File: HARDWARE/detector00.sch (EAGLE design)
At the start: 12 parts, among them IC1 OPT1O1

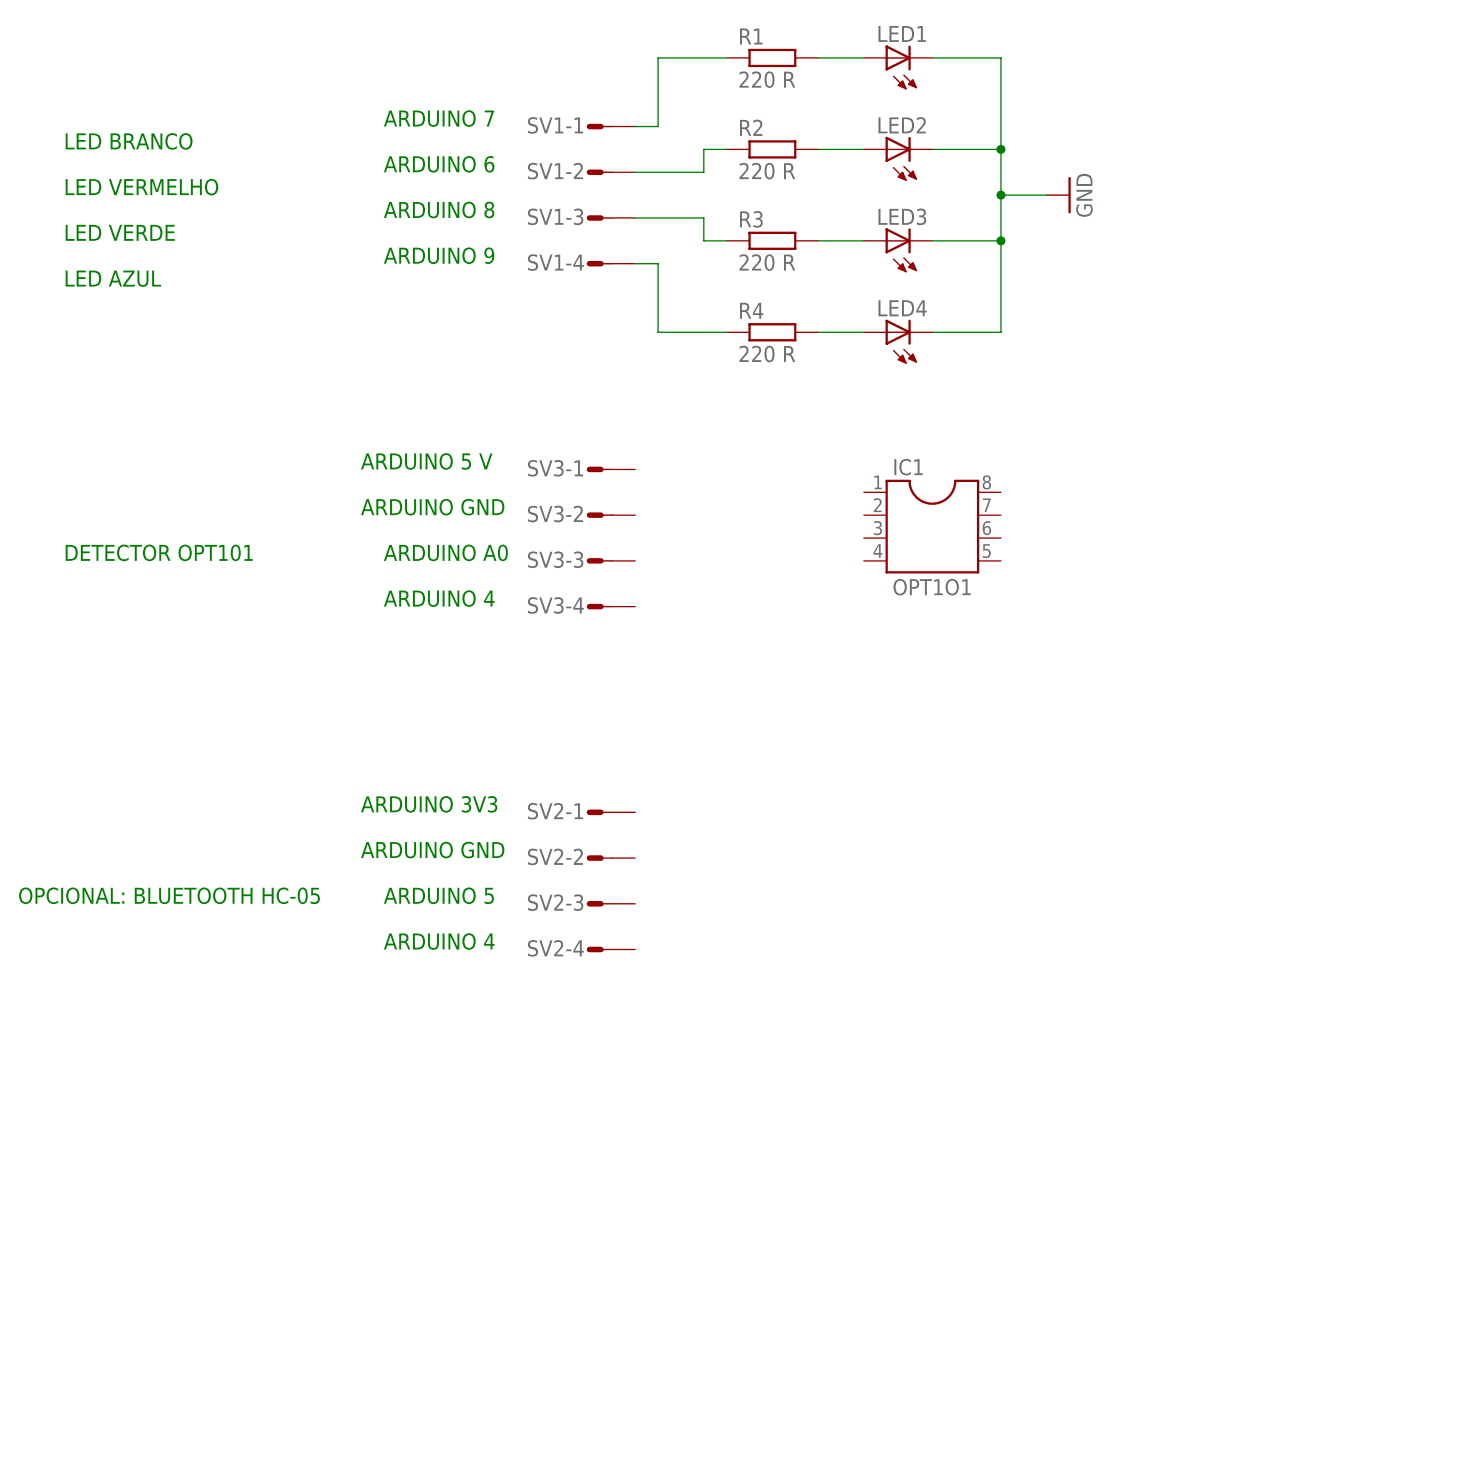
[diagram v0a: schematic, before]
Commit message: Adequações
-proteção ADC
-Correção detector00
-Adição detector05
-Inclusão de teste de tempo de leitura e de conjunto optoeletrônico
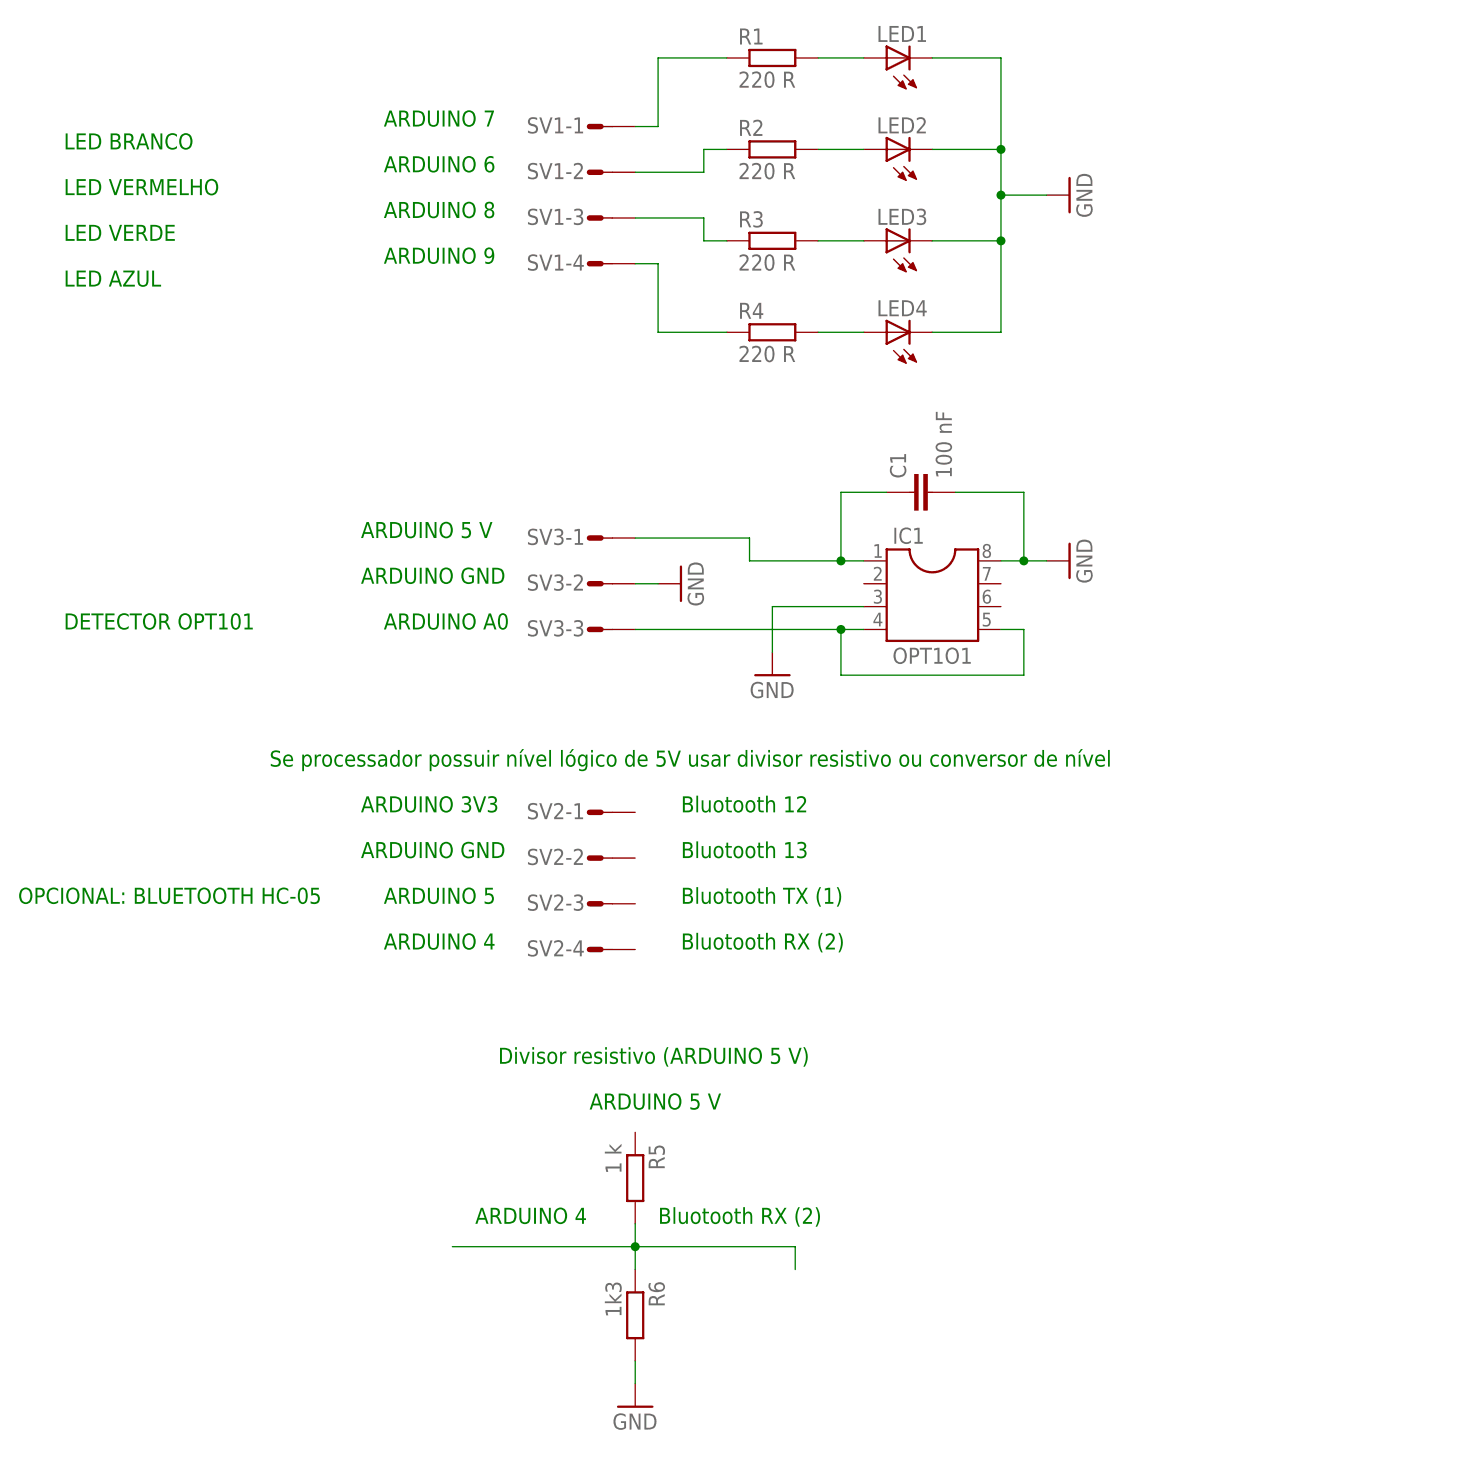
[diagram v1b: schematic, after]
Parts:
- added C1: 100 nF, rcl:C-EU050-035X075
- added R5: 1 k, rcl:R-EU_0204/7
- added R6: 1k3, rcl:R-EU_0204/7
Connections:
- new net N$3: C1.1, IC1.1, SV3-1.S
- new net N$4: R5.2, R6.1
- new net N$8: IC1.4, IC1.5, SV3-3.S
- net GND: now also C1.2, IC1.3, IC1.8, R6.2, SV3-2.S
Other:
- note added: "Bluotooth 12"
- note added: "Bluotooth 13"
- note added: "Bluotooth RX (2)"
- note added: "Bluotooth TX (1)"
- note added: "Divisor resistivo (ARDUINO 5 V)"
- note added: "Se processador possuir nível lógico de 5V usar divisor resistivo ou conversor de nível"
- moved on the sheet: IC1, SV3-1, SV3-2, SV3-3
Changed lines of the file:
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@@
 <part name="GND1" library="supply1" deviceset="GND" device=""/>
 <part name="IC1" library="ic-package" deviceset="DIL8" device="" value="OPT1O1"/>
+<part name="C1" library="rcl" deviceset="C-EU" device="050-035X075" value="100 nF"/>
+<part name="GND2" library="supply1" deviceset="GND" device=""/>
+<part name="GND3" library="supply1" deviceset="GND" device=""/>
+<part name="GND4" library="supply1" deviceset="GND" device=""/>
+<part name="R5" library="rcl" deviceset="R-EU_" device="0204/7" value="1 k"/>
+<part name="R6" library="rcl" deviceset="R-EU_" device="0204/7" value="1k3"/>
+<part name="GND5" library="supply1" deviceset="GND" device=""/>
 </parts>
 <sheets>
@@
 <text x="25.4" y="71.12" size="1.778" layer="91">LED BRANCO</text>
 <text x="25.4" y="60.96" size="1.778" layer="91">LED VERDE</text>
-<text x="58.42" y="35.56" size="1.778" layer="91">ARDUINO 5 V</text>
-<text x="58.42" y="30.48" size="1.778" layer="91">ARDUINO GND</text>
-<text x="60.96" y="25.4" size="1.778" layer="91">ARDUINO A0</text>
-<text x="60.96" y="20.32" size="1.778" layer="91">ARDUINO 4</text>
-<text x="25.4" y="25.4" size="1.778" layer="91">DETECTOR OPT101</text>
+<text x="58.42" y="27.94" size="1.778" layer="91">ARDUINO 5 V</text>
+<text x="58.42" y="22.86" size="1.778" layer="91">ARDUINO GND</text>
+<text x="60.96" y="17.78" size="1.778" layer="91">ARDUINO A0</text>
+<text x="25.4" y="17.78" size="1.778" layer="91">DETECTOR OPT101</text>
 <text x="25.4" y="66.04" size="1.778" layer="91">LED VERMELHO</text>
 <text x="25.4" y="55.88" size="1.778" layer="91">LED AZUL</text>
+<text x="93.98" y="-2.54" size="1.778" layer="91">Bluotooth 12</text>
+<text x="93.98" y="-7.62" size="1.778" layer="91">Bluotooth 13</text>
+<text x="93.98" y="-12.7" size="1.778" layer="91">Bluotooth TX (1)</text>
+<text x="93.98" y="-17.78" size="1.778" layer="91">Bluotooth RX (2)</text>
+<text x="48.26" y="2.54" size="1.778" layer="91">Se processador possuir nível lógico de 5V usar divisor resistivo ou conversor de nível</text>
+<text x="83.82" y="-35.56" size="1.778" layer="91">ARDUINO 5 V</text>
+<text x="71.12" y="-48.26" size="1.778" layer="91">ARDUINO 4</text>
+<text x="91.44" y="-48.26" size="1.778" layer="91">Bluotooth RX (2)</text>
+<text x="73.66" y="-30.48" size="1.778" layer="91">Divisor resistivo (ARDUINO 5 V)</text>
 </plain>
 <instances>
@@
 <instance part="R1" gate="G$1" x="104.14" y="81.28"/>
 <instance part="R2" gate="G$1" x="104.14" y="71.12"/>
-<instance part="SV3" gate="-1" x="83.82" y="35.56"/>
-<instance part="SV3" gate="-2" x="83.82" y="30.48"/>
-<instance part="SV3" gate="-3" x="83.82" y="25.4"/>
-<instance part="SV3" gate="-4" x="83.82" y="20.32"/>
+<instance part="SV3" gate="-1" x="83.82" y="27.94"/>
+<instance part="SV3" gate="-2" x="83.82" y="22.86"/>
+<instance part="SV3" gate="-3" x="83.82" y="17.78"/>
 <instance part="LED3" gate="G$1" x="116.84" y="60.96" rot="R90"/>
 <instance part="LED4" gate="G$1" x="116.84" y="50.8" rot="R90"/>
@@
 <instance part="R4" gate="G$1" x="104.14" y="50.8"/>
 <instance part="GND1" gate="1" x="137.16" y="66.04" rot="R90"/>
-<instance part="IC1" gate="G$1" x="121.92" y="30.48"/>
+<instance part="IC1" gate="G$1" x="121.92" y="22.86"/>
+<instance part="C1" gate="G$1" x="119.38" y="33.02" rot="R90"/>
+<instance part="GND2" gate="1" x="137.16" y="25.4" rot="R90"/>
+<instance part="GND3" gate="1" x="93.98" y="22.86" rot="R90"/>
+<instance part="GND4" gate="1" x="104.14" y="12.7"/>
+<instance part="R5" gate="G$1" x="88.9" y="-43.18" rot="R270"/>
+<instance part="R6" gate="G$1" x="88.9" y="-58.42" rot="R270"/>
+<instance part="GND5" gate="1" x="88.9" y="-68.58"/>
 </instances>
 <busses>
@@
 <junction x="129.54" y="60.96"/>
 </segment>
-</net>
+<segment>
+<pinref part="SV3" gate="-2" pin="S"/>
+<pinref part="GND3" gate="1" pin="GND"/>
+<wire x1="88.9" y1="22.86" x2="91.44" y2="22.86" width="0.1524" layer="91"/>
+</segment>
+<segment>
+<pinref part="C1" gate="G$1" pin="2"/>
+<wire x1="124.46" y1="33.02" x2="132.08" y2="33.02" width="0.1524" layer="91"/>
+<wire x1="132.08" y1="33.02" x2="132.08" y2="25.4" width="0.1524" layer="91"/>
+<pinref part="IC1" gate="G$1" pin="8"/>
+<wire x1="132.08" y1="25.4" x2="129.54" y2="25.4" width="0.1524" layer="91"/>
+<pinref part="GND2" gate="1" pin="GND"/>
+<wire x1="134.62" y1="25.4" x2="132.08" y2="25.4" width="0.1524" layer="91"/>
+<junction x="132.08" y="25.4"/>
+</segment>
+<segment>
+<pinref part="IC1" gate="G$1" pin="3"/>
+<pinref part="GND4" gate="1" pin="GND"/>
+<wire x1="114.3" y1="20.32" x2="104.14" y2="20.32" width="0.1524" layer="91"/>
+<wire x1="104.14" y1="20.32" x2="104.14" y2="15.24" width="0.1524" layer="91"/>
+</segment>
+<segment>
+<pinref part="GND5" gate="1" pin="GND"/>
+<pinref part="R6" gate="G$1" pin="2"/>
+<wire x1="88.9" y1="-66.04" x2="88.9" y2="-63.5" width="0.1524" layer="91"/>
+</segment>
+</net>
+<net name="N$3" class="0">
+<segment>
+<pinref part="C1" gate="G$1" pin="1"/>
+<wire x1="116.84" y1="33.02" x2="111.76" y2="33.02" width="0.1524" layer="91"/>
+<wire x1="111.76" y1="33.02" x2="111.76" y2="25.4" width="0.1524" layer="91"/>
+<pinref part="IC1" gate="G$1" pin="1"/>
+<wire x1="111.76" y1="25.4" x2="114.3" y2="25.4" width="0.1524" layer="91"/>
+<junction x="111.76" y="25.4"/>
+<pinref part="SV3" gate="-1" pin="S"/>
+<wire x1="88.9" y1="27.94" x2="101.6" y2="27.94" width="0.1524" layer="91"/>
+<wire x1="101.6" y1="27.94" x2="101.6" y2="25.4" width="0.1524" layer="91"/>
+<wire x1="101.6" y1="25.4" x2="111.76" y2="25.4" width="0.1524" layer="91"/>
+</segment>
+</net>
+<net name="N$8" class="0">
+<segment>
+<pinref part="IC1" gate="G$1" pin="4"/>
+<wire x1="114.3" y1="17.78" x2="111.76" y2="17.78" width="0.1524" layer="91"/>
+<wire x1="111.76" y1="17.78" x2="111.76" y2="12.7" width="0.1524" layer="91"/>
+<wire x1="111.76" y1="12.7" x2="132.08" y2="12.7" width="0.1524" layer="91"/>
+<wire x1="132.08" y1="12.7" x2="132.08" y2="17.78" width="0.1524" layer="91"/>
+<pinref part="IC1" gate="G$1" pin="5"/>
+<wire x1="132.08" y1="17.78" x2="129.54" y2="17.78" width="0.1524" layer="91"/>
+<pinref part="SV3" gate="-3" pin="S"/>
+<wire x1="88.9" y1="17.78" x2="111.76" y2="17.78" width="0.1524" layer="91"/>
+<junction x="111.76" y="17.78"/>
+</segment>
+</net>
+<net name="N$4" class="0">
+<segment>
+<pinref part="R5" gate="G$1" pin="2"/>
+<pinref part="R6" gate="G$1" pin="1"/>
+<wire x1="88.9" y1="-48.26" x2="88.9" y2="-50.8" width="0.1524" layer="91"/>
+<wire x1="88.9" y1="-50.8" x2="88.9" y2="-53.34" width="0.1524" layer="91"/>
+<wire x1="88.9" y1="-50.8" x2="68.58" y2="-50.8" width="0.1524" layer="91"/>
+<junction x="88.9" y="-50.8"/>
+<wire x1="88.9" y1="-50.8" x2="106.68" y2="-50.8" width="0.1524" layer="91"/>
+<wire x1="106.68" y1="-50.8" x2="106.68" y2="-53.34" width="0.1524" layer="91"/>
+</segment>
+</net>
